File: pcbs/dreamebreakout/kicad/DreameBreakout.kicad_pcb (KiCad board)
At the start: 2 copper layers, 18 x 61.5 mm, 10 parts, among them J1.1 To Robot SoC, J1.2 To Robot MCU, J2 SoC Breakout, J3 MCU Breakout, J4 SoC_FEL_USB, J5 OTG_USB, SW1 SoC_Boot_SEL_BTN

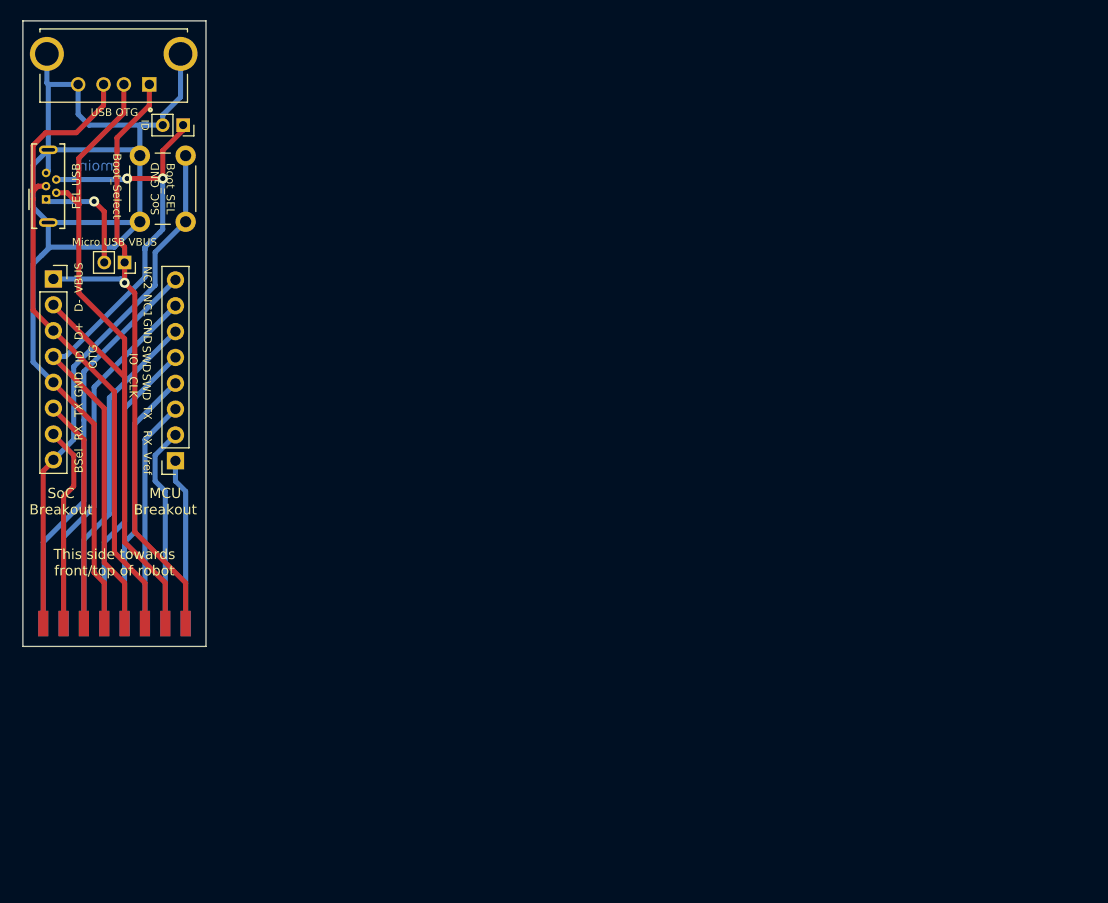
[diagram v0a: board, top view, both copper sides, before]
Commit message: Update original Dreame breakout board
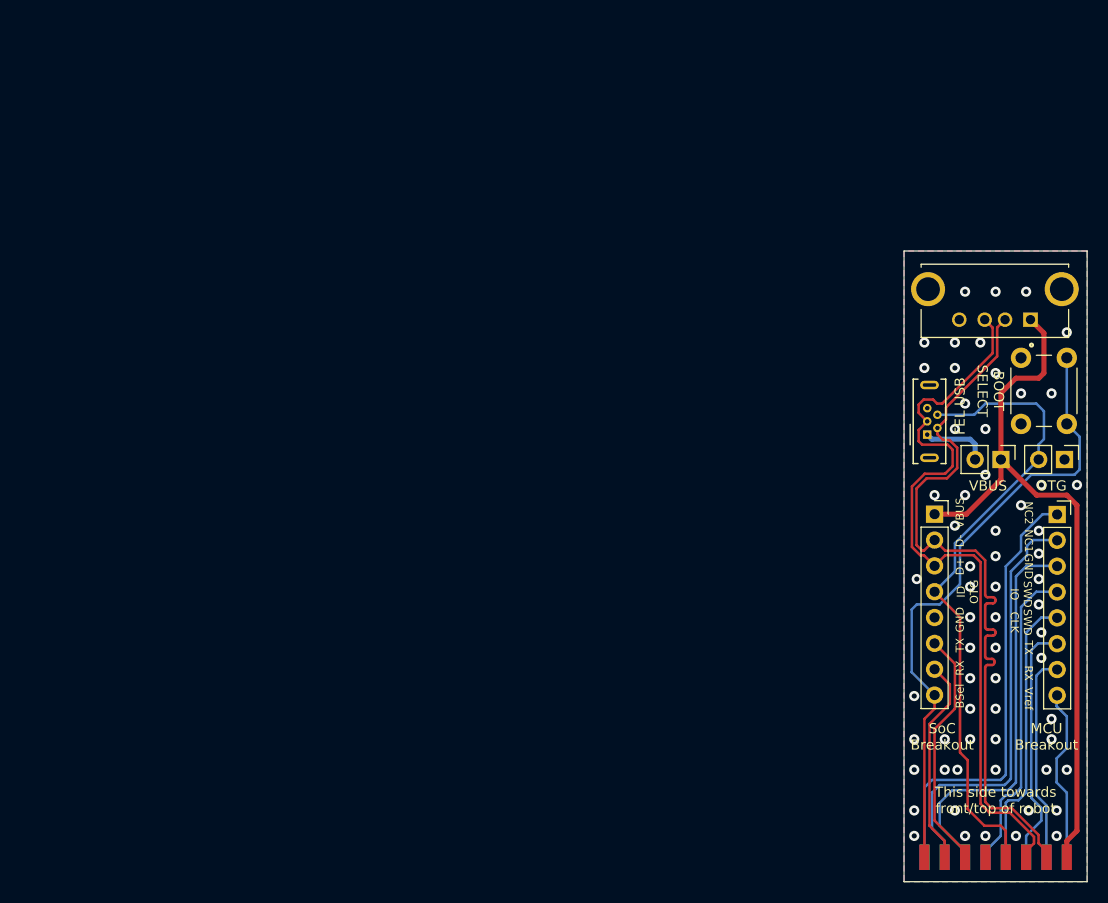
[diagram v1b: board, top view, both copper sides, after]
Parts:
- removed G***: LOGO, Custom:valetudog
- JP1, JP2: footprint Connector_PinSocket_2.00mm:PinSocket_1x02_P2.00mm_Vertical -> Connector_PinHeader_2.54mm:PinHeader_1x02_P2.54mm_Vertical
- moved JP2 92.7 mm to (152.4, 81.9)
- moved J1 89.7 mm to (145.6, 65.1)
- moved J2 89.7 mm to (138.9, 79.4)
- moved J5 89.7 mm to (139.6, 87.2)
- moved J1.1 89.6 mm to (145.6, 121.0)
- moved J1.2 89.6 mm to (145.6, 121.0)
- moved SW1 88.9 mm to (148.1, 78.4)
- moved JP1 88.3 mm to (146.2, 81.9)
- moved J4 86.8 mm to (151.7, 87.3), turned to 0 degrees
- renumbered J5 to J1, J4 to J2, J3 to J4, J2 to J5
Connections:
- net Boot_SEL renamed /Boot_SEL
- net D+ renamed /D+
- net D- renamed /D-
- net SoC_RX renamed /SoC_RX
- net SoC_TX renamed /SoC_TX
- net USB_VBUS renamed /USB_VBUS
- net VBUS renamed /VBUS
- J1 pad 4: SoC_GND -> GND
- J1.1 pad 4: SoC_GND -> GND
- J1.1 pad 5: SoC_USB_OTG_ID -> /SoC_USB_OTG_ID
- J1.2 pad 1: MCU_Vref -> /MCU_Vref
- J1.2 pad 2: MCU_RX -> /MCU_RX
- J1.2 pad 3: MCU_TX -> /MCU_TX
- J1.2 pad 4: MCU_SWCLK -> /MCU_SWCLK
- J1.2 pad 5: MCU_SWDIO -> /MCU_SWDIO
- J1.2 pad 6: MCU_GND -> /MCU_GND
- J1.2 pad 7: MCU_NC1 -> /MCU_NC1
- J1.2 pad 8: MCU_NC2 -> /MCU_NC2
- J2 pad 4: SoC_USB_OTG_ID -> /SoC_USB_OTG_ID
- J2 pad 5: SoC_GND -> GND
- J2 pad 6: SoC_GND -> GND
- J4 pad 1: MCU_Vref -> /MCU_NC2
- J4 pad 2: MCU_RX -> /MCU_NC1
- J4 pad 3: MCU_TX -> /MCU_GND
- J4 pad 4: MCU_SWCLK -> /MCU_SWDIO
- J4 pad 5: MCU_SWDIO -> /MCU_SWCLK
- J4 pad 6: MCU_GND -> /MCU_TX
- J4 pad 7: MCU_NC1 -> /MCU_RX
- J4 pad 8: MCU_NC2 -> /MCU_Vref
- J5 pad 4: SoC_USB_OTG_ID -> /SoC_USB_OTG_ID
- J5 pad 5: SoC_GND -> GND
- JP2 pad 1: SoC_USB_OTG_ID -> GND
- JP2 pad 2: SoC_GND -> /SoC_USB_OTG_ID
- SW1 pad 1: SoC_GND -> GND
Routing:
- net SoC_GND: track 125.0 -> 0.00 mm
- net SoC_USB_OTG_ID: track 68.3 -> 0.00 mm, vias 2 -> 0
- net /SoC_USB_OTG_ID: track 0.00 -> 63.5 mm
- net /MCU_NC2: track 0.00 -> 44.0 mm
- net /MCU_NC1: track 0.00 -> 42.0 mm
- net MCU_NC2: track 39.2 -> 0.00 mm
- net /MCU_GND: track 0.00 -> 38.8 mm
- net MCU_NC1: track 35.8 -> 0.00 mm
- net MCU_GND: track 32.4 -> 0.00 mm
- net /MCU_SWDIO: track 0.00 -> 30.0 mm
- net MCU_SWDIO: track 29.1 -> 0.00 mm
- net /MCU_SWCLK: track 0.00 -> 27.3 mm
- net MCU_SWCLK: track 25.7 -> 0.00 mm
- net /MCU_TX: track 0.00 -> 24.3 mm
- net MCU_TX: track 22.3 -> 0.00 mm
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- added copper zone on B.Cu, net GND
- added copper zone on F.Cu, net GND
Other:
- board size 18 x 61.5 mm -> 18 x 62 mm
- board text added: "0.2500 mm / 0.2000 mm"
- board text added: "0.3500 mm"
- board text added: "1.2000 mm"
- board text added: "18.0000 mm x 62.0000 mm"
- board text added: "2"
- board text added: "Alex Knapik"
- board text added: "BOARD CHARACTERISTICS"
- board text added: "BOOT SELECT"
- board text added: "Board Thickness:"
- board text added: "Board overall dimensions:"
- board text added: "Castellated pads:"
- board text added: "Copper Finish:"
- board text added: "Copper Layer Count:"
- board text added: "Edge card connectors:"
- board text added: "HAL lead-free"
- board text added: "Impedance Control:"
- board text added: "Min hole diameter:"
- board text added: "Min track/spacing:"
- board text added: "No"
- board text added: "OTG"
- board text added: "Plated Board Edge:"
- board text added: "Rev. ${REVISION} ${ISSUE_DATE}"
- board text added: "valetudo.cloud dontvacuum.me"
- board text removed: "Boot_SEL"
- board text removed: "Boot_Select"
- board text removed: "ID"
- board text removed: "Micro USB VBUS"
- board text removed: "Revision 2022.09.0"
- board text removed: "SoC_GND"
- board text removed: "USB OTG"
- board text removed: "dontvacuum.me"
- board text removed: "moin."
- board text removed: "valetudo.cloud"
